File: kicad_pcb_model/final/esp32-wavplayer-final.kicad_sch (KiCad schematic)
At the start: 84 parts, among them SW1 RST, SW2 BOOT, U1 TP4056-42-ESOP8, U3 PCM5102A

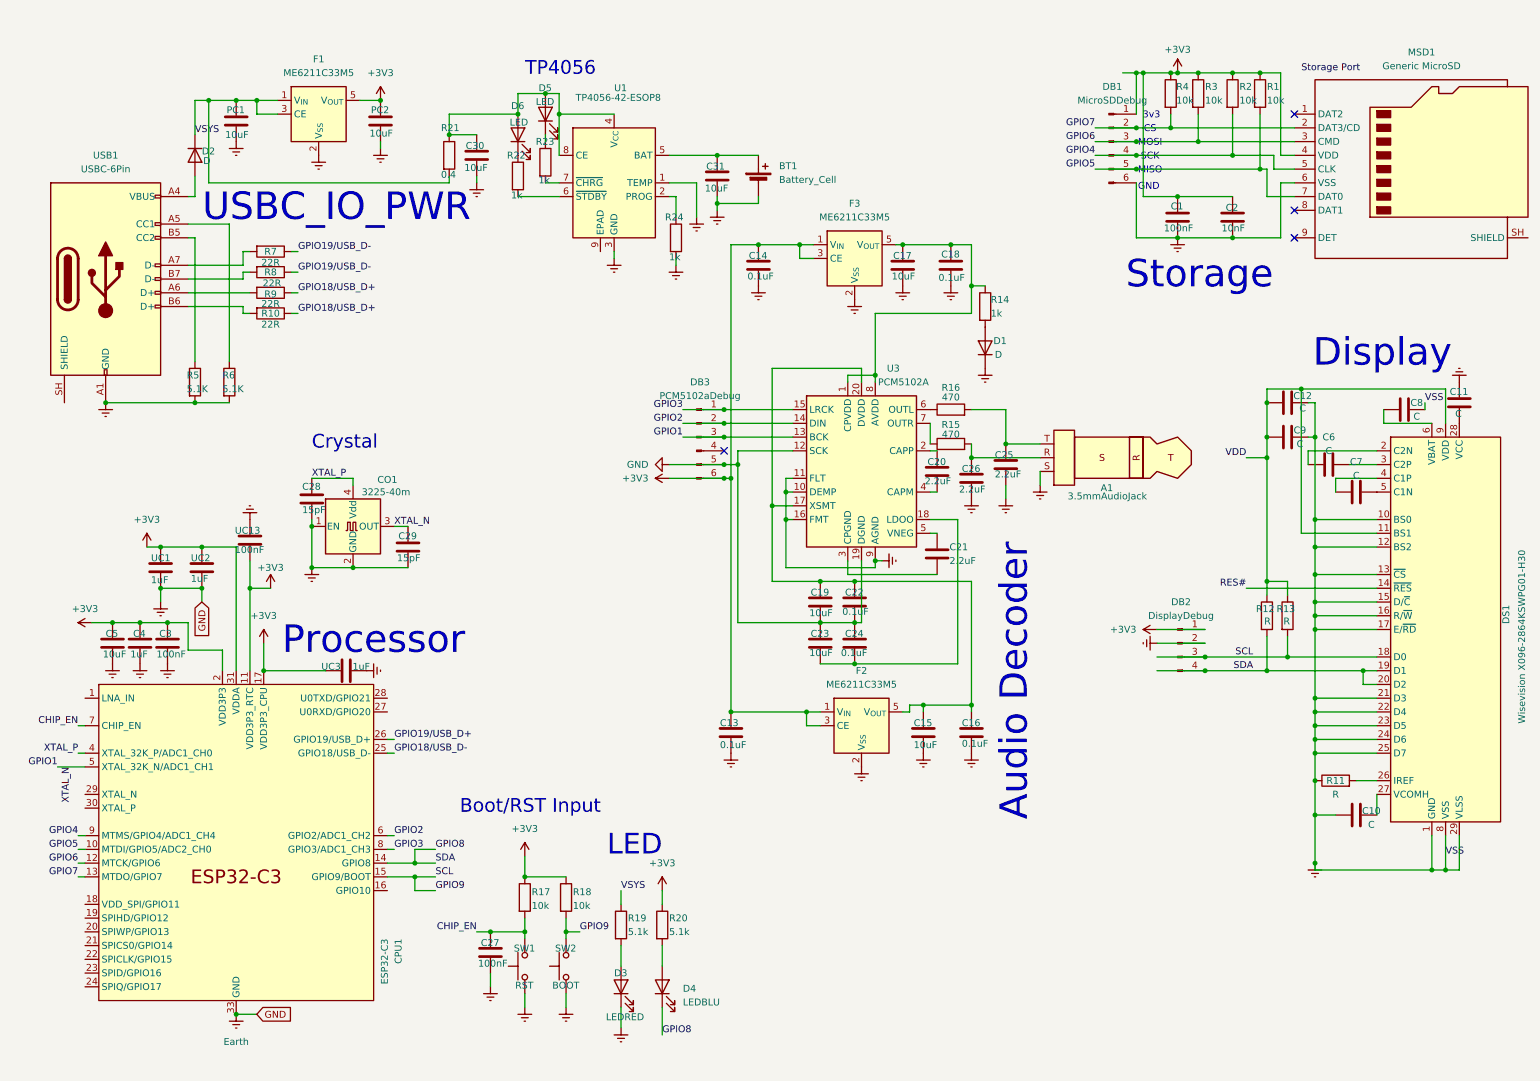
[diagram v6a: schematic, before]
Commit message: Adding battery circuit and updating pcb
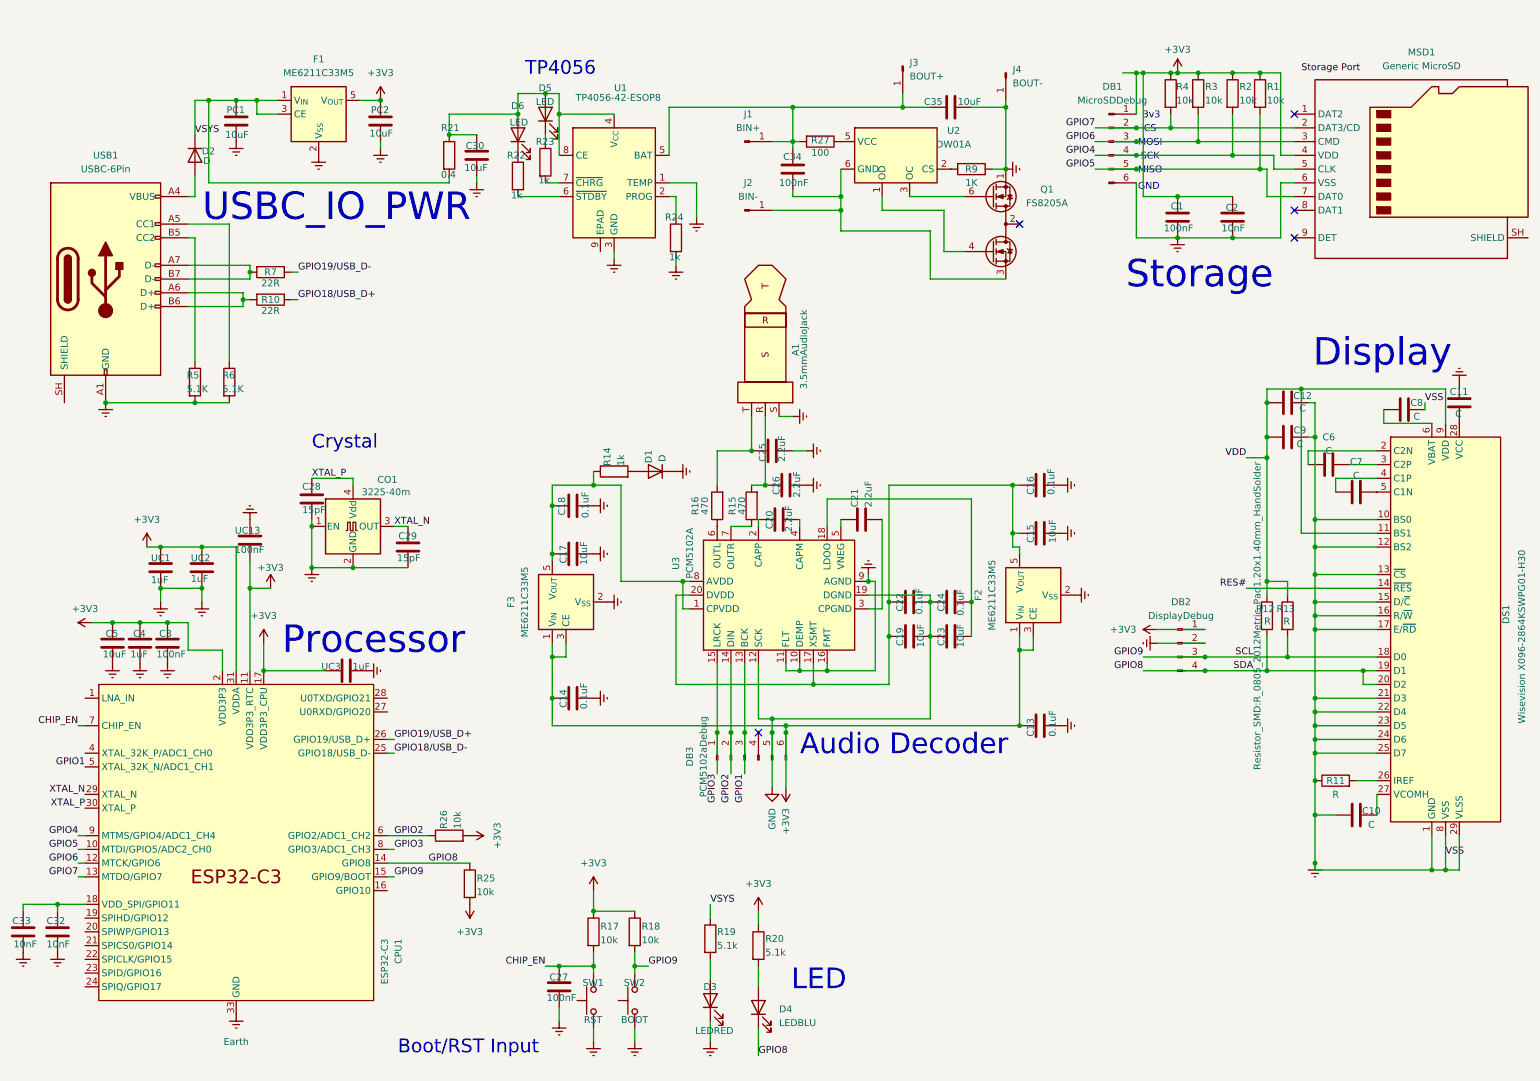
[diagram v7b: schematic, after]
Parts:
- removed BT1: Battery_Cell, Package_TO_SOT_SMD:SOT-23-5, symbol Device:Battery_Cell
- removed C31: 10uF, symbol Device:C
- removed R8: 22R, symbol Device:R
- added C32, C33: 10nF, Capacitor_SMD:C_0805_2012Metric_Pad1.18x1.45mm_HandSolder, symbol Device:C
- added C34: 100nF, Capacitor_SMD:C_0805_2012Metric_Pad1.18x1.45mm_HandSolder, symbol Device:C
- added C35: 10uF, Capacitor_SMD:C_0805_2012Metric_Pad1.18x1.45mm_HandSolder, symbol Device:C
- added J1: BIN+, Connector_PinHeader_2.54mm:PinHeader_1x01_P2.54mm_Vertical, symbol Connector:Conn_01x01_Pin
- added J2: BIN-, Connector_PinHeader_2.54mm:PinHeader_1x01_P2.54mm_Vertical, symbol Connector:Conn_01x01_Pin
- added J3: BOUT+, Connector_PinHeader_2.54mm:PinHeader_1x01_P2.54mm_Vertical, symbol Connector:Conn_01x01_Pin
- added J4: BOUT-, Connector_PinHeader_2.54mm:PinHeader_1x01_P2.54mm_Vertical, symbol Connector:Conn_01x01_Pin
- added Q1: FS8205A, Package_TO_SOT_SMD:SOT-23-6, symbol Transistor_FET:DMG9926UDM
- added R25, R26: 10k, Resistor_SMD:R_0805_2012Metric_Pad1.20x1.40mm_HandSolder, symbol Device:R
- added R27: 100, Resistor_SMD:R_0805_2012Metric_Pad1.20x1.40mm_HandSolder, symbol Device:R
- added U2: DW01A, Package_TO_SOT_SMD:SOT-23-6, symbol Battery_Management:DW01A
- A1: footprint Package_QFP:TQFP-48-1EP_7x7mm_P0.5mm_EP3.5x3.5mm -> Connector_Audio:Jack_3.5mm_KoreanHropartsElec_PJ-320D-4A_Horizontal
- C1, C10, C11, C12, C13, C14, C15, C16, C17, C18, C19, C2, C20, C21, C22, C23, C24, C25, C26, C27, C3, C30, C4, C5, C7, C8, C9, PC2, UC1, UC13, UC2, UC3: footprint (none) -> Capacitor_SMD:C_0805_2012Metric_Pad1.18x1.45mm_HandSolder
- C28, C29: footprint Oscillator:Oscillator_SMD_Abracon_ASE-4Pin_3.2x2.5mm -> Capacitor_SMD:C_0805_2012Metric_Pad1.18x1.45mm_HandSolder
- C6: footprint Display:OLED-128O064D -> Capacitor_SMD:C_0805_2012Metric_Pad1.18x1.45mm_HandSolder
- D1, D2: footprint (none) -> Diode_SMD:D_0805_2012Metric_Pad1.15x1.40mm_HandSolder
- D3, D4: footprint (none) -> LED_SMD:LED_0805_2012Metric_Pad1.15x1.40mm_HandSolder
- D5, D6: footprint Display:OLED-128O064D -> LED_SMD:LED_0805_2012Metric_Pad1.15x1.40mm_HandSolder
- DB1: footprint (none) -> Connector_PinHeader_2.54mm:PinHeader_1x06_P2.54mm_Vertical
- DB2: footprint (none) -> Connector_PinHeader_2.54mm:PinHeader_1x04_P2.54mm_Vertical
- DB3: footprint Package_SO:TSSOP-20_4.4x6.5mm_P0.65mm -> Connector_PinHeader_2.54mm:PinHeader_1x06_P2.54mm_Vertical
- PC1: footprint Package_TO_SOT_SMD:SOT-23-5 -> Capacitor_SMD:C_0805_2012Metric_Pad1.18x1.45mm_HandSolder
- R1, R10, R11, R12, R13, R14, R15, R16, R17, R18, R19, R2, R20, R21, R22, R23, R24, R3, R4, R7: footprint (none) -> Resistor_SMD:R_0805_2012Metric_Pad1.20x1.40mm_HandSolder
- R5, R6: footprint Package_DIP:DIP-8_W7.62mm -> Resistor_SMD:R_0805_2012Metric_Pad1.20x1.40mm_HandSolder
- R9: value 22R -> 1K; footprint (none) -> Resistor_SMD:R_0805_2012Metric_Pad1.20x1.40mm_HandSolder
- SW1: footprint Button_Switch_THT:SW_NKK_GW12LJP -> Button_Switch_SMD:SW_SPST_TS-1088-xR020
- SW2: footprint (none) -> Button_Switch_SMD:SW_SPST_TS-1088-xR020
- USB1: footprint (none) -> Connector_USB:USB_C_Receptacle_HRO_TYPE-C-31-M-12
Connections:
- net +3V3: now also R25.2, R26.2
- net Earth: now also R9.2, C32.2, C33.2, C35.2, J4.1 (Pin_1), Q1.1 (D1); no longer C19.2, C22.2, C23.1, C24.1, DB3.5 (Pin_5), U3.12 (SCK), U3.19 (DGND)
- net GPIO1: no longer C29.1, CO1.3 (OUT)
- net GPIO18/USB_D+: no longer R9.1
- net GPIO2: now also R26.1
- net GPIO8: now also R25.1
- net XTAL_P: now also CPU1.30 (XTAL_P); no longer CPU1.4 (XTAL_32K_P/ADC1_CH0)
- net at USB1.A6 (D+): now also R10.2, USB1.B6 (D+); no longer R9.2
- net at R7.2, USB1.A7 (D-): now also USB1.B7 (D-)
- net at CPU1.18 (VDD_SPI/GPIO11): now also C32.1, C33.1
- net XTAL_N: now reaches CPU1.29 (XTAL_N)
- net XTAL_N: now also C29.1, CO1.3 (OUT)
- net at U1.5 (BAT): now also C34.1, C35.1, J1.1 (Pin_1), J3.1 (Pin_1), R27.2
- new net: Q1.4 (G2), U2.1 (OD)
- new net: R9.1, U2.2 (CS)
- new net: Q1.6 (G1), U2.3 (OC)
- new net: R27.1, U2.5 (VCC)
- new net: C34.2, J2.1 (Pin_1), Q1.3 (S2), U2.6 (GND)
- new net: Q1.2 (S1/D2), Q1.5 (S1/D2)
- new net GND: C19.2, C22.2, C23.1, C24.1, DB3.5 (Pin_5), U3.12 (SCK), U3.19 (DGND)
- no-connect marks 4 -> 5
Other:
- moved on the sheet: A1, C13, C14, C15, C16, C17, C18, C19, C20, C21, C22, C23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

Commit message: Routing PCB
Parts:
- removed C12, C6, C7, C8, C9: C, Capacitor_SMD:C_0805_2012Metric_Pad1.18x1.45mm_HandSolder, symbol Device:C
- removed J3: BOUT+, Connector_PinHeader_2.54mm:PinHeader_1x01_P2.54mm_Vertical, symbol Connector:Conn_01x01_Pin
- removed J4: BOUT-, Connector_PinHeader_2.54mm:PinHeader_1x01_P2.54mm_Vertical, symbol Connector:Conn_01x01_Pin
- added DC2, DC3, DC4, DC5, DC6: C, Capacitor_SMD:C_0603_1608Metric_Pad1.08x0.95mm_HandSolder, symbol Device:C
- AC1: renamed from C13; footprint Capacitor_SMD:C_0805_2012Metric_Pad1.18x1.45mm_HandSolder -> Capacitor_SMD:C_0603_1608Metric_Pad1.08x0.95mm_HandSolder
- AC10: renamed from C18; footprint Capacitor_SMD:C_0805_2012Metric_Pad1.18x1.45mm_HandSolder -> Capacitor_SMD:C_0603_1608Metric_Pad1.08x0.95mm_HandSolder
- AC11: renamed from C20; footprint Capacitor_SMD:C_0805_2012Metric_Pad1.18x1.45mm_HandSolder -> Capacitor_SMD:C_0603_1608Metric_Pad1.08x0.95mm_HandSolder
- AC12: renamed from C26; footprint Capacitor_SMD:C_0805_2012Metric_Pad1.18x1.45mm_HandSolder -> Capacitor_SMD:C_0603_1608Metric_Pad1.08x0.95mm_HandSolder
- AC13: renamed from C25; footprint Capacitor_SMD:C_0805_2012Metric_Pad1.18x1.45mm_HandSolder -> Capacitor_SMD:C_0603_1608Metric_Pad1.08x0.95mm_HandSolder
- AC14: renamed from C21; footprint Capacitor_SMD:C_0805_2012Metric_Pad1.18x1.45mm_HandSolder -> Capacitor_SMD:C_0603_1608Metric_Pad1.08x0.95mm_HandSolder
- AC2: renamed from C15; footprint Capacitor_SMD:C_0805_2012Metric_Pad1.18x1.45mm_HandSolder -> Capacitor_SMD:C_0603_1608Metric_Pad1.08x0.95mm_HandSolder
- AC3: renamed from C16; footprint Capacitor_SMD:C_0805_2012Metric_Pad1.18x1.45mm_HandSolder -> Capacitor_SMD:C_0603_1608Metric_Pad1.08x0.95mm_HandSolder
- AC4: renamed from C22; footprint Capacitor_SMD:C_0805_2012Metric_Pad1.18x1.45mm_HandSolder -> Capacitor_SMD:C_0603_1608Metric_Pad1.08x0.95mm_HandSolder
- AC5: renamed from C19; footprint Capacitor_SMD:C_0805_2012Metric_Pad1.18x1.45mm_HandSolder -> Capacitor_SMD:C_0603_1608Metric_Pad1.08x0.95mm_HandSolder
- AC6: renamed from C24; footprint Capacitor_SMD:C_0805_2012Metric_Pad1.18x1.45mm_HandSolder -> Capacitor_SMD:C_0603_1608Metric_Pad1.08x0.95mm_HandSolder
- AC7: renamed from C23; footprint Capacitor_SMD:C_0805_2012Metric_Pad1.18x1.45mm_HandSolder -> Capacitor_SMD:C_0603_1608Metric_Pad1.08x0.95mm_HandSolder
- AC8: renamed from C14; footprint Capacitor_SMD:C_0805_2012Metric_Pad1.18x1.45mm_HandSolder -> Capacitor_SMD:C_0603_1608Metric_Pad1.08x0.95mm_HandSolder
- AC9: renamed from C17; footprint Capacitor_SMD:C_0805_2012Metric_Pad1.18x1.45mm_HandSolder -> Capacitor_SMD:C_0603_1608Metric_Pad1.08x0.95mm_HandSolder
- AD1: renamed from D1; footprint Diode_SMD:D_0805_2012Metric_Pad1.15x1.40mm_HandSolder -> Diode_SMD:D_0603_1608Metric_Pad1.05x0.95mm_HandSolder
- AR1: renamed from R15; footprint Resistor_SMD:R_0805_2012Metric_Pad1.20x1.40mm_HandSolder -> Resistor_SMD:R_0603_1608Metric_Pad0.98x0.95mm_HandSolder
- AR2: renamed from R16; footprint Resistor_SMD:R_0805_2012Metric_Pad1.20x1.40mm_HandSolder -> Resistor_SMD:R_0603_1608Metric_Pad0.98x0.95mm_HandSolder
- AR3: renamed from R14; footprint Resistor_SMD:R_0805_2012Metric_Pad1.20x1.40mm_HandSolder -> Resistor_SMD:R_0603_1608Metric_Pad0.98x0.95mm_HandSolder
- BC1: renamed from C27; footprint Capacitor_SMD:C_0805_2012Metric_Pad1.18x1.45mm_HandSolder -> Capacitor_SMD:C_0603_1608Metric_Pad1.08x0.95mm_HandSolder
- BR1: renamed from R17; footprint Resistor_SMD:R_0805_2012Metric_Pad1.20x1.40mm_HandSolder -> Resistor_SMD:R_0603_1608Metric_Pad0.98x0.95mm_HandSolder
- BR2: renamed from R18; footprint Resistor_SMD:R_0805_2012Metric_Pad1.20x1.40mm_HandSolder -> Resistor_SMD:R_0603_1608Metric_Pad0.98x0.95mm_HandSolder
- BTM1: renamed from U1; footprint Package_SO:SOIC-8-1EP_3.9x4.9mm_P1.27mm_EP2.41x3.3mm_ThermalVias -> Package_SO:SOIC-8_3.9x4.9mm_P1.27mm
- CC1: renamed from UC1; footprint Capacitor_SMD:C_0805_2012Metric_Pad1.18x1.45mm_HandSolder -> Capacitor_SMD:C_0603_1608Metric_Pad1.08x0.95mm_HandSolder
- CC2: renamed from UC2; footprint Capacitor_SMD:C_0805_2012Metric_Pad1.18x1.45mm_HandSolder -> Capacitor_SMD:C_0603_1608Metric_Pad1.08x0.95mm_HandSolder
- CC3: renamed from UC13; footprint Capacitor_SMD:C_0805_2012Metric_Pad1.18x1.45mm_HandSolder -> Capacitor_SMD:C_0603_1608Metric_Pad1.08x0.95mm_HandSolder
- CC4: renamed from C3; footprint Capacitor_SMD:C_0805_2012Metric_Pad1.18x1.45mm_HandSolder -> Capacitor_SMD:C_0603_1608Metric_Pad1.08x0.95mm_HandSolder
- CC5: renamed from C4; footprint Capacitor_SMD:C_0805_2012Metric_Pad1.18x1.45mm_HandSolder -> Capacitor_SMD:C_0603_1608Metric_Pad1.08x0.95mm_HandSolder
- CC6: renamed from C5; footprint Capacitor_SMD:C_0805_2012Metric_Pad1.18x1.45mm_HandSolder -> Capacitor_SMD:C_0603_1608Metric_Pad1.08x0.95mm_HandSolder
- CC7: renamed from UC3; footprint Capacitor_SMD:C_0805_2012Metric_Pad1.18x1.45mm_HandSolder -> Capacitor_SMD:C_0603_1608Metric_Pad1.08x0.95mm_HandSolder
- CC8: renamed from C33; footprint Capacitor_SMD:C_0805_2012Metric_Pad1.18x1.45mm_HandSolder -> Capacitor_SMD:C_0603_1608Metric_Pad1.08x0.95mm_HandSolder
- CC9: renamed from C32; footprint Capacitor_SMD:C_0805_2012Metric_Pad1.18x1.45mm_HandSolder -> Capacitor_SMD:C_0603_1608Metric_Pad1.08x0.95mm_HandSolder
- CR1: renamed from R25; footprint Resistor_SMD:R_0805_2012Metric_Pad1.20x1.40mm_HandSolder -> Resistor_SMD:R_0603_1608Metric_Pad0.98x0.95mm_HandSolder
- CR2: renamed from R26; footprint Resistor_SMD:R_0805_2012Metric_Pad1.20x1.40mm_HandSolder -> Resistor_SMD:R_0603_1608Metric_Pad0.98x0.95mm_HandSolder
- CR3: renamed from R7; footprint Resistor_SMD:R_0805_2012Metric_Pad1.20x1.40mm_HandSolder -> Resistor_SMD:R_0603_1608Metric_Pad0.98x0.95mm_HandSolder
- CR4: renamed from R10; footprint Resistor_SMD:R_0805_2012Metric_Pad1.20x1.40mm_HandSolder -> Resistor_SMD:R_0603_1608Metric_Pad0.98x0.95mm_HandSolder
- D3: value LEDRED -> PWRLED; footprint LED_SMD:LED_0805_2012Metric_Pad1.15x1.40mm_HandSolder -> LED_SMD:LED_0603_1608Metric_Pad1.05x0.95mm_HandSolder
- D4: value LEDBLU -> ONLED; footprint LED_SMD:LED_0805_2012Metric_Pad1.15x1.40mm_HandSolder -> LED_SMD:LED_0603_1608Metric_Pad1.05x0.95mm_HandSolder
- D5: value LED -> CHRGLED; footprint LED_SMD:LED_0805_2012Metric_Pad1.15x1.40mm_HandSolder -> LED_SMD:LED_0603_1608Metric_Pad1.05x0.95mm_HandSolder
- D6: value LED -> STNDLED; footprint LED_SMD:LED_0805_2012Metric_Pad1.15x1.40mm_HandSolder -> LED_SMD:LED_0603_1608Metric_Pad1.05x0.95mm_HandSolder
- DC1: renamed from C11; footprint Capacitor_SMD:C_0805_2012Metric_Pad1.18x1.45mm_HandSolder -> Capacitor_SMD:C_0603_1608Metric_Pad1.08x0.95mm_HandSolder
- DC7: renamed from C10; footprint Capacitor_SMD:C_0805_2012Metric_Pad1.18x1.45mm_HandSolder -> Capacitor_SMD:C_0603_1608Metric_Pad1.08x0.95mm_HandSolder
- DR1: renamed from R12; footprint Resistor_SMD:R_0805_2012Metric_Pad1.20x1.40mm_HandSolder -> Resistor_SMD:R_0603_1608Metric_Pad0.98x0.95mm_HandSolder
- DR2: renamed from R13; footprint Resistor_SMD:R_0805_2012Metric_Pad1.20x1.40mm_HandSolder -> Resistor_SMD:R_0603_1608Metric_Pad0.98x0.95mm_HandSolder
- DR3: renamed from R11; footprint Resistor_SMD:R_0805_2012Metric_Pad1.20x1.40mm_HandSolder -> Resistor_SMD:R_0603_1608Metric_Pad0.98x0.95mm_HandSolder
- LR1: renamed from R19; footprint Resistor_SMD:R_0805_2012Metric_Pad1.20x1.40mm_HandSolder -> Resistor_SMD:R_0603_1608Metric_Pad0.98x0.95mm_HandSolder
- LR2: renamed from R20; footprint Resistor_SMD:R_0805_2012Metric_Pad1.20x1.40mm_HandSolder -> Resistor_SMD:R_0603_1608Metric_Pad0.98x0.95mm_HandSolder
- MSD1: footprint Module:Maple_Mini -> Connector_Card:microSD_HC_Hirose_DM3AT-SF-PEJM5
- OC1: renamed from C28; footprint Capacitor_SMD:C_0805_2012Metric_Pad1.18x1.45mm_HandSolder -> Capacitor_SMD:C_0603_1608Metric_Pad1.08x0.95mm_HandSolder
- OC2: renamed from C29; footprint Capacitor_SMD:C_0805_2012Metric_Pad1.18x1.45mm_HandSolder -> Capacitor_SMD:C_0603_1608Metric_Pad1.08x0.95mm_HandSolder
- PC1, PC2: footprint Capacitor_SMD:C_0805_2012Metric_Pad1.18x1.45mm_HandSolder -> Capacitor_SMD:C_0603_1608Metric_Pad1.08x0.95mm_HandSolder
- PC3: renamed from C30; footprint Capacitor_SMD:C_0805_2012Metric_Pad1.18x1.45mm_HandSolder -> Capacitor_SMD:C_0603_1608Metric_Pad1.08x0.95mm_HandSolder
- PC4: renamed from C34; footprint Capacitor_SMD:C_0805_2012Metric_Pad1.18x1.45mm_HandSolder -> Capacitor_SMD:C_0603_1608Metric_Pad1.08x0.95mm_HandSolder
- PC5: renamed from C35; footprint Capacitor_SMD:C_0805_2012Metric_Pad1.18x1.45mm_HandSolder -> Capacitor_SMD:C_0603_1608Metric_Pad1.08x0.95mm_HandSolder
- PD1: renamed from D2; footprint Diode_SMD:D_0805_2012Metric_Pad1.15x1.40mm_HandSolder -> Diode_SMD:D_0603_1608Metric_Pad1.05x0.95mm_HandSolder
- PR1: renamed from R5; footprint Resistor_SMD:R_0805_2012Metric_Pad1.20x1.40mm_HandSolder -> Resistor_SMD:R_0603_1608Metric_Pad0.98x0.95mm_HandSolder
- PR2: renamed from R6; footprint Resistor_SMD:R_0805_2012Metric_Pad1.20x1.40mm_HandSolder -> Resistor_SMD:R_0603_1608Metric_Pad0.98x0.95mm_HandSolder
- PR3: renamed from R21; footprint Resistor_SMD:R_0805_2012Metric_Pad1.20x1.40mm_HandSolder -> Resistor_SMD:R_0603_1608Metric_Pad0.98x0.95mm_HandSolder
- PR4: renamed from R22; footprint Resistor_SMD:R_0805_2012Metric_Pad1.20x1.40mm_HandSolder -> Resistor_SMD:R_0603_1608Metric_Pad0.98x0.95mm_HandSolder
- PR5: renamed from R23; footprint Resistor_SMD:R_0805_2012Metric_Pad1.20x1.40mm_HandSolder -> Resistor_SMD:R_0603_1608Metric_Pad0.98x0.95mm_HandSolder
- PR6: renamed from R24; footprint Resistor_SMD:R_0805_2012Metric_Pad1.20x1.40mm_HandSolder -> Resistor_SMD:R_0603_1608Metric_Pad0.98x0.95mm_HandSolder
- PR7: renamed from R27; footprint Resistor_SMD:R_0805_2012Metric_Pad1.20x1.40mm_HandSolder -> Resistor_SMD:R_0603_1608Metric_Pad0.98x0.95mm_HandSolder
- PR8: renamed from R9; footprint Resistor_SMD:R_0805_2012Metric_Pad1.20x1.40mm_HandSolder -> Resistor_SMD:R_0603_1608Metric_Pad0.98x0.95mm_HandSolder
- SC1: renamed from C1; footprint Capacitor_SMD:C_0805_2012Metric_Pad1.18x1.45mm_HandSolder -> Capacitor_SMD:C_0603_1608Metric_Pad1.08x0.95mm_HandSolder
- SC2: renamed from C2; footprint Capacitor_SMD:C_0805_2012Metric_Pad1.18x1.45mm_HandSolder -> Capacitor_SMD:C_0603_1608Metric_Pad1.08x0.95mm_HandSolder
- SR1: renamed from R1; footprint Resistor_SMD:R_0805_2012Metric_Pad1.20x1.40mm_HandSolder -> Resistor_SMD:R_0603_1608Metric_Pad0.98x0.95mm_HandSolder
- SR2: renamed from R2; footprint Resistor_SMD:R_0805_2012Metric_Pad1.20x1.40mm_HandSolder -> Resistor_SMD:R_0603_1608Metric_Pad0.98x0.95mm_HandSolder
- SR3: renamed from R3; footprint Resistor_SMD:R_0805_2012Metric_Pad1.20x1.40mm_HandSolder -> Resistor_SMD:R_0603_1608Metric_Pad0.98x0.95mm_HandSolder
- SR4: renamed from R4; footprint Resistor_SMD:R_0805_2012Metric_Pad1.20x1.40mm_HandSolder -> Resistor_SMD:R_0603_1608Metric_Pad0.98x0.95mm_HandSolder
- renumbered F3 to AVR1, F2 to AVR2, U2 to BATPROT1, Q1 to BMFT1, CO1 to CYOC1, F1 to PDVR1
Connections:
- net GND is gone; now on net Earth: AC4.2, AC5.2, AC6.1, AC7.1, DB3.5 (Pin_5), U3.12 (SCK), U3.19 (DGND)
- net +3V3: now also BTM1.5 (BAT), J1.1 (Pin_1), PC4.1, PC5.1, PR7.2
- net Earth: now also DC2.2, DC3.2, DC4.1
- net VDD: now also DC3.1, DC4.2
- net at DS1.6 (VBAT): now also DC2.1
- net at DS1.2 (C2N): now also DC5.1
- net at DS1.3 (C2P): now also DC5.2
- net at DS1.4 (C1P): now also DC6.1
- net at DS1.5 (C1N): now also DC6.2
